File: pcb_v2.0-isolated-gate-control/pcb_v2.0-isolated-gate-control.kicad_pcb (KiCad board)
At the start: 2 copper layers, 160 parts, among them J1 ServoLock, J10 sw, J11 sense, J12 Screw_Terminal_01x06, J13 Relay contacts [NO, COM, NC], J14 sw, J15 sense, J16 sense, J17 sense, J18 sense, J2 sw, J3 sw, J4 sense, J5 sw, J6 sw, J7 Relay contacts [NO, COM, NC], J8 RS485, J9 limit, K1 RT314A24, K2 RT314A24, Q1 2N7000, Q3 IRF5305, Q6 IRF5305, U1 esp32-devkit-v1_30Pin, U4 MAX485E, U5 L78S05CV_TO220, U6 ULN2803A

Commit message: pcb: Optinmize/protect PWM out, Start Layout (arrange as schematic)
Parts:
- added C5: 100uF, Capacitor_THT:CP_Radial_D18.0mm_P7.50mm, F.Cu at (25.1, 53.5)
- added D1: TVS 12V, Diode_THT:D_DO-41_SOD81_P12.70mm_Horizontal, F.Cu at (250.4, 77.7)
- added F2: F-Servo, misc_libJonny:Fuseholder_Automotive-Regular_Fuse19x5x18mm_Footprint21x8mm_Inline, F.Cu at (267.1, 68.1)
- added Q2: 2N7000, Package_TO_SOT_THT:TO-92_HandSolder, F.Cu at (268.5, 79.2)
- added R2: 200, Resistor_THT:R_Axial_DIN0207_L6.3mm_D2.5mm_P10.16mm_Horizontal, F.Cu at (260.9, 73.7)
- added R3: 2k2, Resistor_THT:R_Axial_DIN0207_L6.3mm_D2.5mm_P10.16mm_Horizontal, F.Cu at (248.2, 73.7)
- D13: moved to B.Cu
- J10: value sw -> Buttons
- J11: value sense -> 2x encoder
- J13: value Relay contacts [NO, COM, NC] -> Relay VFD2 [NO, COM, NC]
- J14, J5: value sw -> GND-P
- J15: value sense -> Power-Servo-12V
- J16: value sense -> Power-LightBarrier-12V
- J17: value sense -> 3V3 5V VDD
- J18: value sense -> GNDD
- J2: value sw -> supply
- J3: value sw -> 12V-filtered
- J4: value sense -> light-barrier, reserve
- J6: value sw -> 2x remoteControl
- J7: value Relay contacts [NO, COM, NC] -> Relay VFD1 [NO, COM, NC]
- moved J15 346.2 mm to (394.7, 107.8), turned to 90 degrees
- moved J16 346.2 mm to (395.0, 128.1), turned to 90 degrees
- moved J7 336.7 mm to (392.9, 42.0), turned to 90 degrees
- moved J13 334.8 mm to (392.7, 72.2), turned to 90 degrees
- moved JP3 313.2 mm to (370.0, 52.9)
- moved JP2 304.7 mm to (369.0, 87.9)
- moved JP1 296.2 mm to (363.3, 120.9)
- moved K2 295.7 mm to (385.5, 52.9), turned to 90 degrees
- moved K1 293.5 mm to (385.5, 87.4), turned to 90 degrees
- moved R84 288.7 mm to (381.8, 129.4), turned to 90 degrees
- moved R13 285.7 mm to (348.6, 120.6)
- moved R83 283.3 mm to (380.1, 108.7), turned to 90 degrees
- moved Q6 267.6 mm to (387.5, 125.8), turned to 90 degrees
- moved Q3 264.0 mm to (385.8, 105.5), turned to 90 degrees
- moved D27 260.6 mm to (377.1, 134.1)
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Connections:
- C1 pad 1: +12V filtered -> +12V
- C10 pad 1: +12V filtered -> +12V
- C3 pad 1: +12V filtered -> +12V
- C8 pad 1: +12V filtered -> +12V
- D13 pad 1: RS485_A -> RS485_B
- D13 pad 2: RS485_B -> RS485_A
- D2 pad 1: +12V filtered -> +12V
- D22 pad 1: +12V filtered -> +12V
- D24 pad 1: +12V filtered -> +12V
- D26 pad 2: +12V filtered -> GNDPWR
- D27 pad 2: +12V filtered -> GNDPWR
- D3 pad 2: +12V filtered -> +12V
- J1 pad 1: unconnected-(J1-Pin_1-Pad1) -> GNDPWR
- J1 pad 3: GNDPWR -> Net-(J1-Pin_3)
- J3 pad 1: +12V filtered -> +12V
- J3 pad 2: +12V filtered -> +12V
- K1 pad A1: +12V filtered -> +12V
- K2 pad A1: +12V filtered -> +12V
- OC21 pad 1: +3V3 -> Net-(OC21-Pad1)
- OC21 pad 2: Net-(OC21-Pad2) -> GND
- OC21 pad 4: Net-(J1-Pin_2) -> Net-(Q2-G)
- PS1 pad 2: +12V filtered -> +12V
- Q3 pad 3: +12V filtered -> +12V
- Q6 pad 3: +12V filtered -> +12V
- R11 pad 2: +12V filtered -> +12V
- R13 pad 2: +12V filtered -> +12V
- R76 pad 2: Net-(OC21-Pad2) -> Net-(OC21-Pad1)
- R77 pad 2: Net-(J1-Pin_2) -> Net-(Q2-G)
- R83 pad 2: +12V filtered -> +12V
- R84 pad 2: +12V filtered -> +12V
- U5 pad 1: +12V filtered -> +12V
- U6 pad 10: +12V filtered -> +12V
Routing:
- net Net-(C16-Pad1): track 0.00 -> 15.6 mm
- net /isolated-digital-input_sw-to-gnd5/in_switchToGND: track 0.00 -> 12.9 mm
- net +12V: track 0.00 -> 6.20 mm
- net GNDPWR: track 0.00 -> 3.64 mm
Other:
- board outline added: 160 x 100 mm
- copper layers 2 -> 4

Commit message: pcb: change footprints + arrange groups individually for saving space
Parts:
- removed R11: 2.5, Resistor_THT:R_Axial_DIN0922_L20.0mm_D9.0mm_P25.40mm_Horizontal
- added D22: D, Diode_THT:D_T-1_P12.70mm_Horizontal, F.Cu at (344.8, 96.3)
- added D24: D, Diode_THT:D_T-1_P12.70mm_Horizontal, F.Cu at (357.4, 65.5)
- added J13: Relay VFD2 [NO, COM, NC], TerminalBlock:TerminalBlock_bornier-3_P5.08mm, F.Cu at (378.6, 93.2)
- added J7: Relay VFD1 [NO, COM, NC], TerminalBlock:TerminalBlock_bornier-3_P5.08mm, F.Cu at (377.3, 77.6)
- added JP2: Jumper_2_Bridged, Jumper_AKL:Jumper_P2.54mm_D0.7mm, F.Cu at (342.0, 94.3)
- added JP3: Jumper_2_Bridged, Jumper_AKL:Jumper_P2.54mm_D0.7mm, F.Cu at (342.0, 68.9)
- added K1: RT314A24, Relay_THT:Relay_SPDT_Schrack-RT1-16A-FormC_RM5mm, F.Cu at (346.1, 91.6)
- added K2: RT314A24, Relay_THT:Relay_SPDT_Schrack-RT1-16A-FormC_RM5mm, F.Cu at (346.1, 77.9)
- D26, D27: footprint Diode_THT_AKL_Double:D_DO-27_P20.32mm_Horizontal -> Diode_THT:D_DO-201_P5.08mm_Vertical_KathodeUp
- R1, R10, R27, R30, R39, R40, R41, R42, R45, R48, R51, R54, R57, R60, R63, R65, R66, R67, R68, R70, R71, R72, R75, R76, R80, R81, R82: footprint Resistor_THT:R_Axial_DIN0207_L6.3mm_D2.5mm_P10.16mm_Horizontal -> Resistor_THT:R_Axial_DIN0207_L6.3mm_D2.5mm_P2.54mm_Vertical
- moved R82 238.8 mm to (105.5, 84.5), turned to 90 degrees
- moved R72 238.6 mm to (105.5, 78.8), turned to 90 degrees
- moved R68 238.4 mm to (105.5, 73.1), turned to 90 degrees
- moved R66 238.4 mm to (105.5, 66.8), turned to 90 degrees
- moved R41 238.3 mm to (105.5, 61.1), turned to 90 degrees
- moved R39 238.2 mm to (105.5, 55.5), turned to 90 degrees
- moved OC23 229.0 mm to (92.3, 82.2)
- moved OC19 228.8 mm to (92.2, 76.3)
- moved OC18 228.7 mm to (92.2, 70.5)
- moved OC17 228.6 mm to (92.2, 64.6)
- moved OC16 228.5 mm to (92.2, 58.8)
- moved OC6 228.3 mm to (92.2, 53.1)
- moved R67 220.9 mm to (87.0, 72.8)
- moved R65 220.8 mm to (86.9, 66.9)
- moved R40 220.7 mm to (86.9, 61.3)
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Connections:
- F1 pad 2: Net-(F1-Pad2) -> +12V
- J8 pad 1: GND -> GNDPWR
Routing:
- net +12V: track 6.20 -> 144.9 mm
- net +3V3: track 0.00 -> 120.5 mm
- net +5VA: track 0.00 -> 51.0 mm
- net Net-(J13-Pin_1): track 0.00 -> 45.6 mm
- net GNDPWR: track 3.64 -> 44.8 mm
- net Net-(J13-Pin_2): track 0.00 -> 39.4 mm
- net Net-(J13-Pin_3): track 0.00 -> 29.8 mm
- net Net-(U4-DI): track 0.00 -> 19.0 mm
- net Net-(C16-Pad1): track 15.6 -> 0.00 mm
- net Net-(C18-Pad1): track 0.00 -> 15.4 mm
- net Net-(U4-DE): track 0.00 -> 14.9 mm
- net Net-(C23-Pad1): track 0.00 -> 14.3 mm
- net RS485_B: track 0.00 -> 14.1 mm
- net Net-(C22-Pad1): track 0.00 -> 14.1 mm
- net /isolated-digital-input_sw-to-gnd11/in_switchToGND: track 0.00 -> 13.2 mm
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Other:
- board size 160 x 100 mm -> 165 x 100 mm

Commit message: pcb: arrange almost all groups inside 100x165 pcb
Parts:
- removed the D22 at (193.4, 92.2)
- removed the D24 at (193.4, 62.5)
- removed the J13 at (195.6, 87.9)
- removed J15: Power-Servo-12V, TerminalBlock:TerminalBlock_bornier-2_P5.08mm
- removed the J7 at (195.8, 62.8)
- removed the JP2 at (198.1, 97.8)
- removed the JP3 at (197.7, 69.0)
- removed the K1 at (188.4, 103.1)
- removed the K2 at (188.3, 73.7)
- F1, F2: footprint misc_libJonny:Fuseholder_Automotive-Regular_Fuse19x5x18mm_Footprint21x8mm_Inline -> misc_libJonny:Fuseholder_Automotive-Mini_Fuse11x4x16_Footprint15x5_Inline
- R2: footprint Resistor_THT:R_Axial_DIN0207_L6.3mm_D2.5mm_P10.16mm_Horizontal -> Resistor_THT:R_Axial_DIN0207_L6.3mm_D2.5mm_P2.54mm_Vertical
- moved J13 182.7 mm to (196.1, 82.9)
- moved JP2 182.5 mm to (160.5, 75.4)
- moved K2 181.9 mm to (164.8, 63.1)
- moved J7 181.8 mm to (196.0, 64.5)
- moved D24 181.4 mm to (175.9, 67.4)
- moved K1 181.4 mm to (164.9, 81.6)
- moved JP3 180.8 mm to (161.5, 58.5)
- moved D22 170.9 mm to (176.0, 69.5), turned to 180 degrees
- moved F2 92.6 mm to (189.5, 103.0)
- moved J1 86.7 mm to (195.7, 103.0)
- moved R77 84.4 mm to (174.5, 98.6), turned to 0 degrees
- moved R30 84.3 mm to (99.7, 79.7)
- moved OC3 84.3 mm to (106.2, 76.7)
- moved OC4 84.3 mm to (96.9, 66.5)
- moved OC5 84.3 mm to (100.3, 76.7)
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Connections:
- net Net-(J1-Pin_2) renamed /Servo-PWM-Signal
- F2 pad 1: Net-(J1-Pin_3) -> Net-(J1-Pin_1)
- F2 pad 2: +BATT -> Net-(D26-K)
- J1 pad 1: GNDPWR -> Net-(J1-Pin_1)
- J1 pad 3: Net-(J1-Pin_3) -> GNDPWR
- K1 pad 11: Net-(J13-Pin_2) -> Net-(J13-Pin_3)
- K1 pad 14: Net-(J13-Pin_3) -> Net-(J13-Pin_2)
- K2 pad 11: Net-(J7-Pin_2) -> Net-(J7-Pin_3)
- K2 pad 14: Net-(J7-Pin_3) -> Net-(J7-Pin_2)
- Q3 pad 3: +12V -> +BATT
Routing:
- net /dIn_Encoder2: track 0.00 -> 65.6 mm
- net /dIn_Encoder1: track 0.00 -> 56.9 mm
- net /dIn_Reserve: track 0.00 -> 47.0 mm
- net /dIn_LightBarrier: track 0.00 -> 37.8 mm
- net /dIn_Gate1-Open: track 0.00 -> 28.2 mm
- net Net-(J7-Pin_1): track 0.00 -> 26.8 mm
- net Net-(J13-Pin_2): track 39.4 -> 13.4 mm
- net Net-(J7-Pin_3): track 0.00 -> 21.6 mm
- net Net-(Q2-G): track 0.00 -> 21.3 mm
- net Net-(U4-DI): track 19.0 -> 0.00 mm
- net Net-(J13-Pin_1): track 45.6 -> 27.1 mm
- net /dIn_Gate1-Closed: track 0.00 -> 18.3 mm
- net Net-(U4-DE): track 14.9 -> 0.00 mm
- net Net-(J7-Pin_2): track 0.00 -> 13.5 mm
- net Net-(D1-K): track 0.00 -> 10.9 mm
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
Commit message: pcb: Re-assign FP, Optimize arrangement, Proof-of-concept routing
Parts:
- removed J9: limit, TerminalBlock_Phoenix:TerminalBlock_Phoenix_MKDS-1,5-4_1x04_P5.00mm_Horizontal
- removed R13: 10, Resistor_THT:R_Axial_DIN0207_L6.3mm_D2.5mm_P10.16mm_Horizontal
- added J15: OD, terminals_libJonny:ScrewTerminal_P5mm_2Pin_FP10x8, F.Cu at (196.8, 51.1)
- added J19: OD, terminals_libJonny:ScrewTerminal_P5mm_2Pin_FP10x8, F.Cu at (196.8, 41.1)
- added J20: OD, terminals_libJonny:ScrewTerminal_P5mm_2Pin_FP10x8, F.Cu at (196.8, 61.1)
- added J21: limit-g1, terminals_libJonny:ScrewTerminal_P5mm_2Pin_FP10x8, F.Cu at (87.6, 125.8)
- added R11: 2.5, resistors_libJonny:Cement-Power-R_L22_W10_P23_Horizontal, F.Cu at (183.7, 44.5)
- C1: footprint Capacitor_THT:CP_Radial_D18.0mm_P7.50mm -> Capacitor_THT:CP_Radial_D10.0mm_P3.80mm
- D1: footprint Diode_THT:D_DO-41_SOD81_P12.70mm_Horizontal -> Diode_THT:D_5W_P5.08mm_Vertical_AnodeUp
- J1, J13, J7, J8: footprint TerminalBlock:TerminalBlock_bornier-3_P5.08mm -> terminals_libJonny:ScrewTerminal_P5mm_3Pin_FP15x8
- J10, J11, J14, J16, J17, J18, J2, J3, J4, J5, J6: footprint TerminalBlock:TerminalBlock_bornier-2_P5.08mm -> terminals_libJonny:ScrewTerminal_P5mm_2Pin_FP10x8
- J12: value Screw_Terminal_01x06 -> limit-g2; footprint TerminalBlock_RND:TerminalBlock_RND_205-00016_1x06_P5.00mm_Horizontal -> terminals_libJonny:ScrewTerminal_P5mm_2Pin_FP10x8
- R3, R31, R32, R33, R34: footprint Resistor_THT:R_Axial_DIN0207_L6.3mm_D2.5mm_P10.16mm_Horizontal -> Resistor_THT:R_Axial_DIN0207_L6.3mm_D2.5mm_P2.54mm_Vertical
- moved D24 64.9 mm to (160.0, 130.3), turned to 90 degrees
- moved J7 64.5 mm to (195.8, 129.0)
- moved K2 64.5 mm to (164.6, 127.6)
- moved J12 58.4 mm to (97.6, 125.8)
- moved JP3 56.8 mm to (163.1, 115.3), turned to 0 degrees
- moved D26 45.4 mm to (171.2, 77.8)
- moved D22 44.3 mm to (160.5, 111.0), turned to 90 degrees
- moved Q3 40.3 mm to (166.6, 77.2)
- moved R83 40.1 mm to (161.7, 79.9)
- moved BZ1 37.9 mm to (170.7, 87.4), turned to -90 degrees
- moved D27 36.8 mm to (189.5, 84.9)
- moved J16 36.8 mm to (196.6, 90.6)
- moved Q6 36.8 mm to (184.9, 90.1)
- moved R84 36.8 mm to (179.8, 93.1)
- moved JP1 30.6 mm to (162.1, 88.4), turned to -90 degrees
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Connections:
- BZ1 pad 1: Net-(BZ1-+) -> +12V
- C1 pad 2: GND -> GNDPWR
- C10 pad 2: GND -> GNDPWR
- C19 pad 2: GND -> GNDPWR
- C20 pad 2: GND -> GNDPWR
- C3 pad 2: GND -> GNDPWR
- D2 pad 2: GND -> GNDPWR
- D3 pad 1: GND -> +12V
- D3 pad 2: +12V -> GNDPWR
- F1 pad 2: +12V -> Net-(F1-Pad2)
- J12 pad 1: Net-(J12-Pin_1) -> /isolated-digital-input_sw-to-gnd1/in_switchToGND
- J12 pad 2: Net-(J12-Pin_2) -> /isolated-digital-input_sw-to-gnd/in_switchToGND
- JP1 pad 1: Net-(J12-Pin_6) -> Net-(J15-Pin_1)
- JP2 pad 1: Net-(J12-Pin_2) -> Net-(J20-Pin_2)
- JP3 pad 1: Net-(J12-Pin_1) -> Net-(J20-Pin_1)
- Q3 pad 1: Net-(J12-Pin_3) -> Net-(J19-Pin_1)
- Q6 pad 1: Net-(J12-Pin_5) -> Net-(J15-Pin_2)
- R83 pad 1: Net-(J12-Pin_3) -> Net-(J19-Pin_1)
- R84 pad 1: Net-(J12-Pin_5) -> Net-(J15-Pin_2)
- U5 pad 2: GND -> GNDPWR
- U6 pad 13: Net-(J12-Pin_6) -> Net-(J20-Pin_1)
- U6 pad 14: Net-(J12-Pin_5) -> Net-(J20-Pin_2)
- U6 pad 15: Net-(J12-Pin_4) -> Net-(J15-Pin_1)
- U6 pad 16: Net-(J12-Pin_3) -> Net-(J15-Pin_2)
- U6 pad 17: Net-(J12-Pin_2) -> Net-(J19-Pin_1)
- U6 pad 18: Net-(J12-Pin_1) -> Net-(J19-Pin_2)
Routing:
- net +12V: track 144.9 -> 489.1 mm
- net +5VA: track 43.2 -> 248.2 mm
- net +3V3: track 120.5 -> 234.4 mm
- net Net-(J15-Pin_2): track 0.00 -> 112.7 mm, vias 0 -> 1
- net Net-(J20-Pin_1): track 0.00 -> 102.5 mm, vias 0 -> 1
- net Net-(J19-Pin_1): track 0.00 -> 90.9 mm, vias 0 -> 1
- net Net-(J20-Pin_2): track 0.00 -> 86.4 mm, vias 0 -> 1
- net Net-(J15-Pin_1): track 0.00 -> 83.7 mm, vias 0 -> 1
- net /dOut_ServoPWM: track 0.00 -> 64.9 mm
- net Net-(J19-Pin_2): track 0.00 -> 62.9 mm, vias 0 -> 1
- net /dOut_Buzzer: track 0.00 -> 61.2 mm
- net GNDPWR: track 44.8 -> 102.4 mm
- net /dOut_EnLightBarriers: track 0.00 -> 56.7 mm
- net +BATT: track 0.00 -> 54.4 mm
- net Net-(U6-I1): track 0.00 -> 49.8 mm
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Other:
- board size 165 x 100 mm -> 170 x 110 mm
- board text added: "F-Control"
- board text added: "F-Servo"

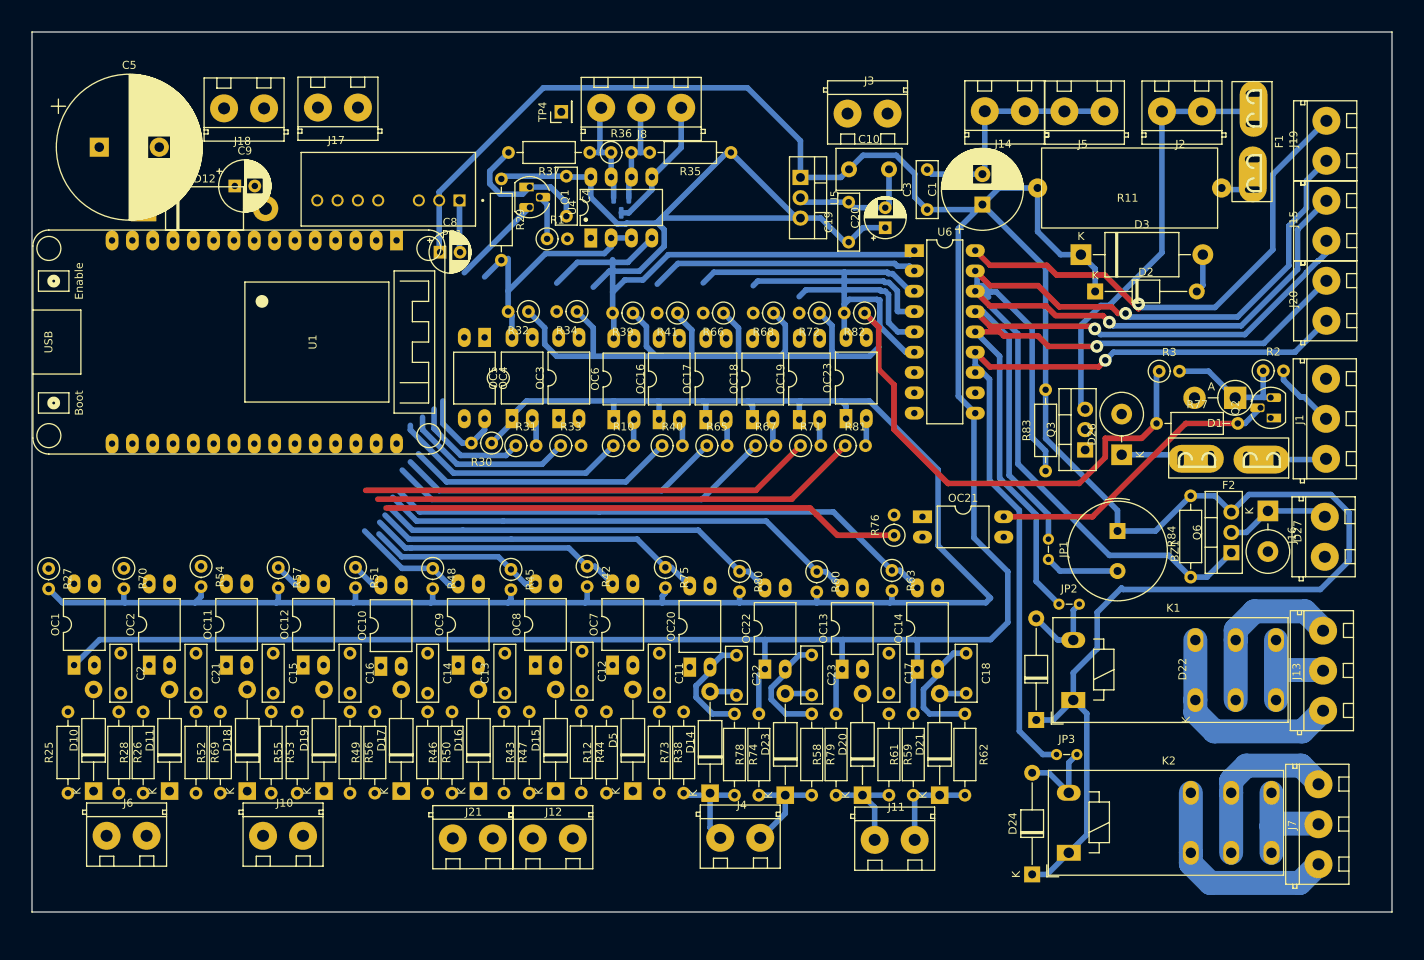
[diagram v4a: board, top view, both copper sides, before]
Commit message: pcb: remap gpio-pins, finish proof-of-concept routing (to evaluate arrangement)
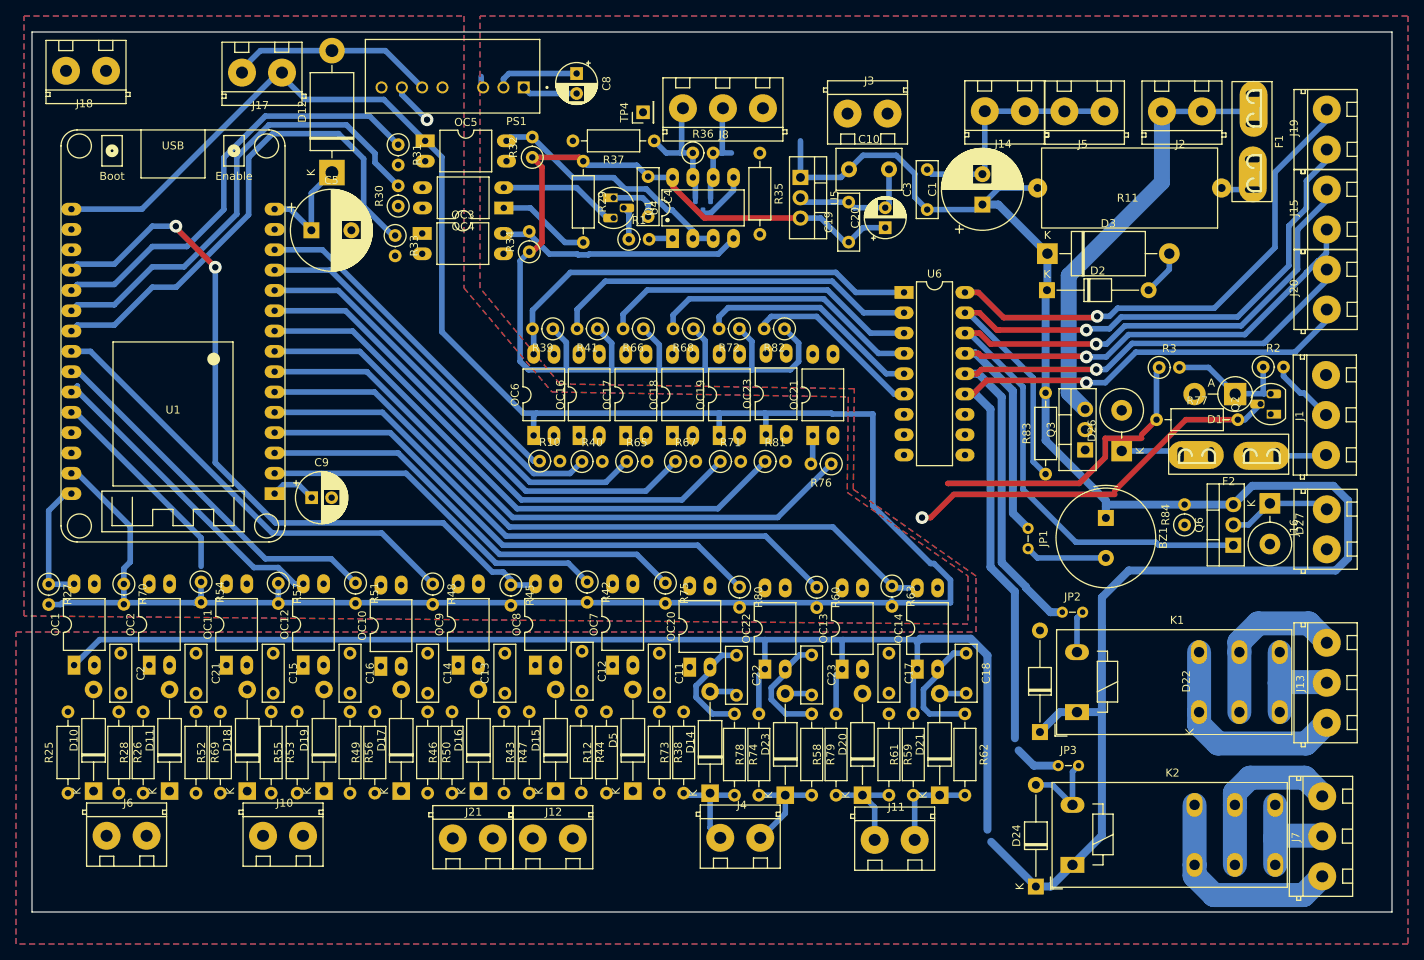
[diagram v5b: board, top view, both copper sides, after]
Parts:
- C5: value 100uF -> 330uF; footprint Capacitor_THT:CP_Radial_D18.0mm_P7.50mm -> Capacitor_THT:CP_Radial_D10.0mm_P5.00mm
- R84: footprint Resistor_THT:R_Axial_DIN0207_L6.3mm_D2.5mm_P10.16mm_Horizontal -> Resistor_THT:R_Axial_DIN0207_L6.3mm_D2.5mm_P2.54mm_Vertical
- moved R31 40.4 mm to (80.8, 39.1), turned to -90 degrees
- moved C9 40.1 mm to (70.0, 83.2)
- moved OC5 36.4 mm to (84.2, 38.6), turned to 0 degrees
- moved U1 33.8 mm to (52.6, 82.7), turned to 180 degrees
- moved R33 33.4 mm to (80.4, 50.4), turned to -90 degrees
- moved R30 31.8 mm to (80.8, 46.8), turned to 90 degrees
- moved OC3 28.8 mm to (83.8, 50.2), turned to 0 degrees
- moved C5 28.5 mm to (69.9, 49.8)
- moved C8 28.1 mm to (103.1, 30.2), turned to -90 degrees
- moved D12 24.0 mm to (72.5, 42.6), turned to 90 degrees
- moved J18 20.3 mm to (44.2, 29.9)
- moved R32 19.3 mm to (97.5, 40.7), turned to 90 degrees
- moved OC21 17.1 mm to (132.6, 75.4), turned to 90 degrees
- moved OC4 16.4 mm to (94.0, 47.0), turned to 180 degrees
- moved PS1 16.2 mm to (87.6, 30.5)
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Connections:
- R10 pad 1: /dOut_RelayEnVFD1 -> /dOut_LED
- R40 pad 1: /dOut_RelayEnVFD2 -> /dOut_RelayEnServo
- R65 pad 1: /dOut_RelayEnServo -> /dOut_EnLightBarriers
- R67 pad 1: /dOut_LED -> /dOut_Buzzer
- R71 pad 1: /dOut_EnLightBarriers -> /dOut_RelayEnVFD2
- R81 pad 1: /dOut_Buzzer -> /dOut_RelayEnVFD1
- U1 pad 10: /dIn_Encoder2 -> /dOut_Buzzer
- U1 pad 12: /dOut_RelayEnVFD2 -> /dOut_RelayEnServo
- U1 pad 13: /dOut_RelayEnVFD1 -> /dOut_LED
- U1 pad 18: /dOut_LED -> unconnected-(U1-GPIO15/HSPI_CS/MTDO/[HIGH-AT-BOOT]-Pad18)
- U1 pad 19: /dIn_RemoteOpen -> /dIn_Gate1-Closed
- U1 pad 23: /dIn_LightBarrier -> /dIn_Gate2-Open
- U1 pad 24: /dIn_Reserve -> /dIn_Gate2-Closed
- U1 pad 25: /dOut_ServoPWM -> /dIn_ButtonClose
- U1 pad 26: /dOut_Buzzer -> /dIn_ButtonOpen
- U1 pad 29: /dOut_RelayEnServo -> /dIn_RemoteClose
- U1 pad 3: /dIn_Gate1-Closed -> /dIn_LightBarrier
- U1 pad 30: unconnected-(U1-GPIO23/VSPI-MOSI-Pad30) -> /dIn_RemoteOpen
- U1 pad 4: /dIn_Gate2-Open -> /dIn_Reserve
- U1 pad 5: /dIn_Gate2-Closed -> /dIn_Encoder1
- U1 pad 6: /dIn_ButtonOpen -> /dIn_Encoder2
- U1 pad 7: /dIn_ButtonClose -> /dOut_ServoPWM
- U1 pad 8: /dIn_RemoteClose -> /dOut_RelayEnVFD1
- U1 pad 9: /dIn_Encoder1 -> /dOut_RelayEnVFD2
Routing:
- net +12V: track 489.1 -> 394.8 mm
- net /dIn_Gate1-Closed: track 22.1 -> 93.7 mm, vias 0 -> 2
- net +5VA: track 248.2 -> 184.8 mm
- net +3V3: track 234.4 -> 294.0 mm
- net /RS485-UART_RX_INVERTED: track 11.1 -> 58.5 mm
- net /dIn_Gate2-Open: track 14.4 -> 57.2 mm
- net /dIn_Gate2-Closed: track 4.09 -> 46.5 mm
- net /dOut_RelayEnVFD1: track 29.6 -> 71.9 mm
- net /RS485-UART_TX: track 21.6 -> 63.8 mm
- net /RS485-UART_DIR-T: track 14.6 -> 55.2 mm
- net /dIn_ButtonClose: track 3.96 -> 39.9 mm
- net /dOut_RelayEnVFD2: track 33.8 -> 66.5 mm
- net /dIn_ButtonOpen: track 0.00 -> 26.3 mm
- net +5V: track 0.00 -> 26.0 mm
- net /dIn_Encoder2: track 69.7 -> 90.5 mm
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- added copper zone on B.Cu, net GND
- added copper zone on F.Cu, net GND
- added copper zone on B.Cu, net GNDPWR
- added copper zone on F.Cu, net GNDPWR
